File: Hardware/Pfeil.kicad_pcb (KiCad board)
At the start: 4 copper layers, 50 x 13 mm, 49 parts, among them IC1 2536030320001, IC2 AP7312-1233FM-7, J3 TagConnect, U2 WSEN-PADS_2511020213301, U3 WSEN-PADS_2511020213301, U4 nRF52840, X2 XTAL 32.768kHz 9pF, X3 XTAL 32MHz 8pF

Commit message: Luca Berthold review
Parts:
- removed X3: XTAL 32MHz 8pF, Crystal:Crystal_SMD_2016-4Pin_2.0x1.6mm
- added X1: XTAL 32MHz 8pF, Crystal:Crystal_SMD_2016-4Pin_2.0x1.6mm, F.Cu at (134.8, 53.5)
- moved C7 3.60 mm to (170.8, 55.6), turned to 90 degrees
- moved C40 3.57 mm to (141.1, 52.9)
- moved C43 3.57 mm to (141.6, 53.4)
- moved C49 3.08 mm to (144.4, 53.9)
- moved C47 2.95 mm to (138.1, 52.9)
- moved C46 2.77 mm to (132.8, 59.4), turned to 45 degrees
- moved L5 2.57 mm to (144.9, 55.0), turned to 135 degrees
- moved C39 2.26 mm to (135.2, 55.8), turned to 45 degrees
- moved C10 2.03 mm to (159.0, 61.8)
- moved C11 2.03 mm to (159.0, 62.5)
- moved C12 2.03 mm to (163.8, 61.4)
- moved IC2 2.03 mm to (161.4, 62.0)
- moved ANT1 1.73 mm to (151.9, 53.1)
- moved C29 1.73 mm to (147.6, 54.0)
- moved C4 1.73 mm to (147.6, 53.2)
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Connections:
- C7 pad 1: /ISDS_INT_00 -> /VDD_IO
- IC1 pad 1: /ISDS_INT_00 -> /SAO
- IC1 pad 10: /RSVD0 -> unconnected-(IC1-RSVD_3-Pad10)
- IC1 pad 11: /RSVD1 -> unconnected-(IC1-RSVD_4-Pad11)
- IC1 pad 2: /ISDS_INT_00 -> /RSVD3
- IC1 pad 3: /ISDS_INT_00 -> /RSVD2
- IC1 pad 5: /ISDS_INT_00 -> /VDD_IO
- R5 pad 1: /ISDS_INT_00 -> /VDD_IO
- R5 pad 2: /ISDS_INT_00 -> /RSVD2
- R6 pad 1: /ISDS_INT_00 -> /VDD_IO
- R6 pad 2: /ISDS_INT_00 -> /RSVD3
- R7 pad 1: /ISDS_INT_00 -> /VDD_IO
- R7 pad 2: /ISDS_INT_00 -> /SAO
- R9 pad 1: /ISDS_INT -> /VDD_IO
- R9 pad 2: /ISDS_INT_00 -> /ISDS_INT
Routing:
- net GND: track 94.9 -> 11.3 mm, vias 12 -> 61
- net /ISDS_INT_00: track 15.1 -> 0.00 mm, vias 2 -> 0
- net /VDD_IO: track 0.00 -> 13.9 mm, vias 0 -> 2
- net /I2C_SDA A1: track 25.0 -> 16.7 mm
- net /I2C_SDA A2: track 30.3 -> 27.2 mm
- net +3V3: track 72.4 -> 69.5 mm
- net /FEEL: track 14.4 -> 12.3 mm
- net Net-(U4-XC1): track 2.89 -> 5.02 mm
- net Net-(U4-DEC6): track 3.89 -> 1.84 mm
- net Net-(U4-XC2): track 6.07 -> 4.19 mm
- net /RSVD2: track 0.00 -> 1.85 mm
- net /SAO: track 0.00 -> 1.83 mm
- net Net-(U4-DEC3): track 4.13 -> 2.53 mm
- net /RSVD3: track 0.00 -> 1.49 mm
- net Net-(U4-DEC2): track 1.64 -> 2.73 mm
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- added copper zone on B.Cu, net GND
- added copper zone on F.Cu, net GND
- added copper zone on In1.Cu, net GND
- added copper zone on In2.Cu, net GND
- removed copper zone on B.Cu, net (none)
- removed copper zone on F.Cu, net (none)
- removed copper zone on In1.Cu, net (none)
- removed copper zone on In2.Cu, net (none)

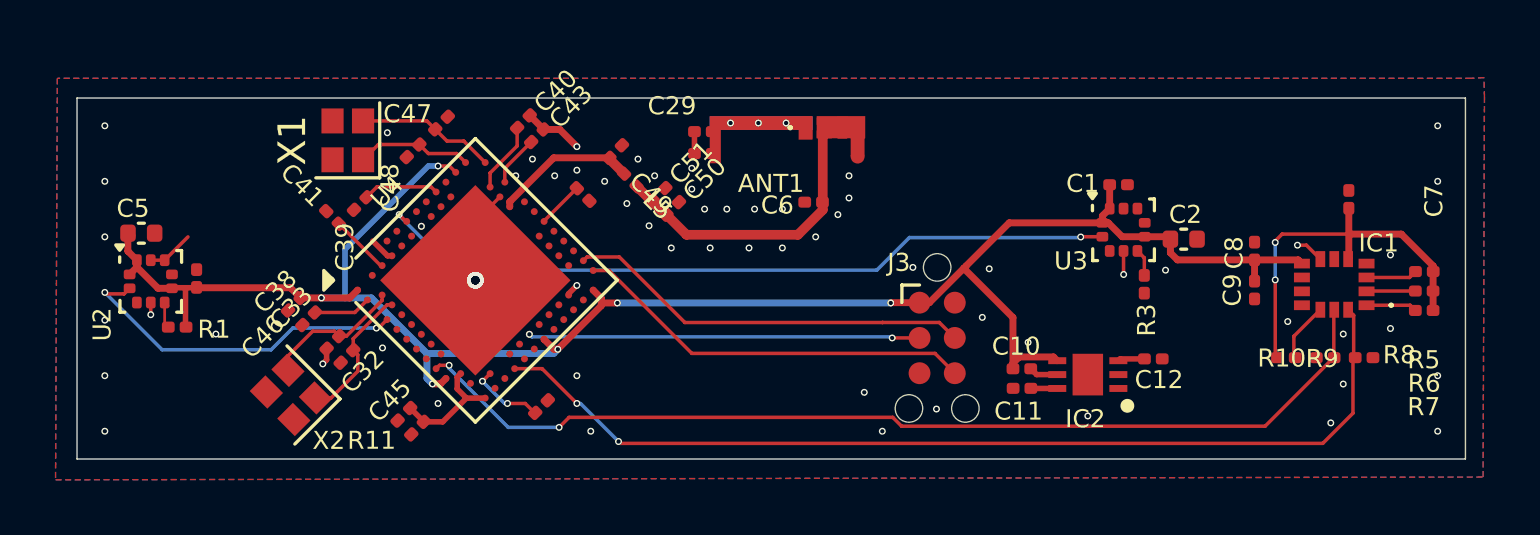
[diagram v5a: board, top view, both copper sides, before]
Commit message: Fix all sikscreen erros
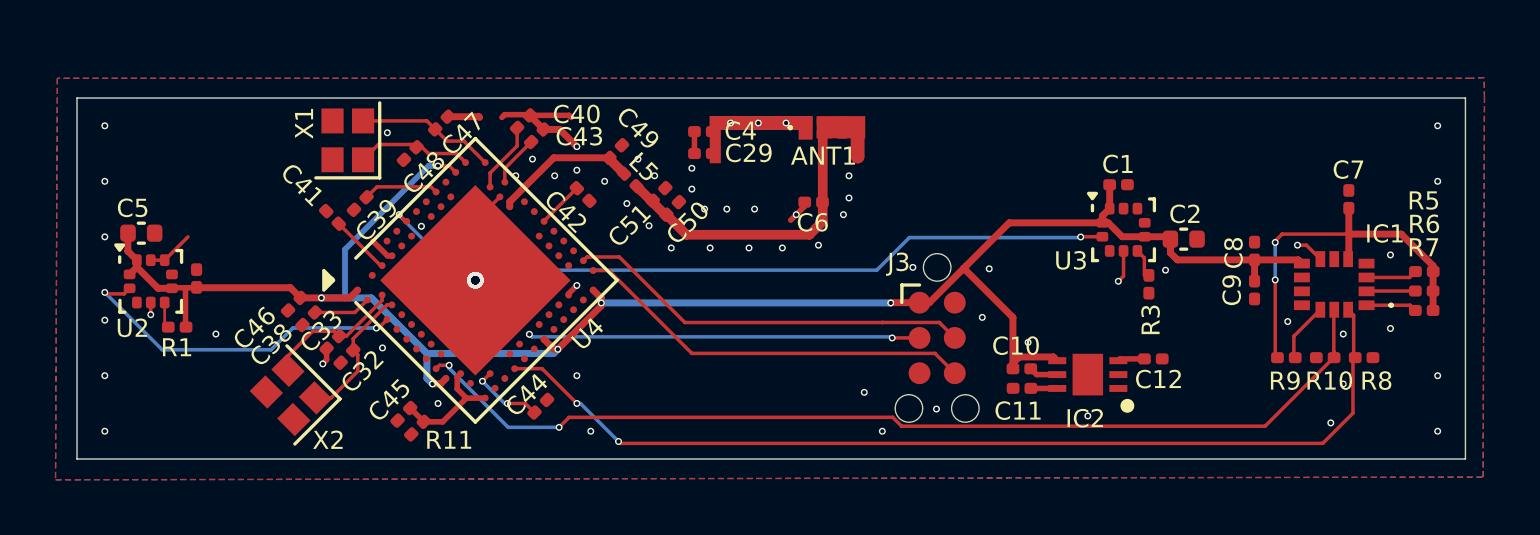
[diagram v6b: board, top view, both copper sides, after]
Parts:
- moved R3 0.16 mm to (163.6, 58.7)
- moved C48 0.14 mm to (137.0, 54.0)
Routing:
- net GND: track 11.3 -> 15.9 mm

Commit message: Bestellte version
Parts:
- added C13: 1uF, Capacitor_SMD:C_0805_2012Metric, F.Cu at (165.1, 62.5)
- added J1: Conn_01x01_Pin, Connector_Wire:SolderWirePad_1x01_SMD_1x2mm, B.Cu at (173.8, 63.1)
- added J2: Conn_01x01_Pin, Connector_Wire:SolderWirePad_1x01_SMD_1x2mm, F.Cu at (173.8, 63.1)
- C10, C11, C12: footprint Capacitor_SMD:C_0201_0603Metric -> Capacitor_SMD:C_0805_2012Metric
- C49: value 100nF -> N.C.
- C50: value 100nF -> 0.5pF NPO +10%
- C51: value 100nF -> 0.8pF NPO +10%
- L5: value L -> 4.7nH 5% HF; footprint Inductor_SMD:L_0201_0603Metric -> LED_SMD:LED_0402_1005Metric
- moved J3 6.71 mm to (149.3, 60.0), turned to 180 degrees
- moved C11 2.71 mm to (161.7, 62.9), turned to 0 degrees
- moved C12 1.61 mm to (165.1, 60.5)
- moved IC2 1.30 mm to (161.7, 60.7)
- moved NT1 0.85 mm to (153.7, 53.0), turned to 180 degrees
- moved C10 0.55 mm to (159.0, 61.2), turned to 90 degrees
- moved C50 0.47 mm to (146.8, 56.3)
- moved C51 0.47 mm to (146.3, 55.8)
- moved L5 0.27 mm to (145.2, 55.1)
- moved C49 0.06 mm to (144.4, 54.0)
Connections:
- IC2 pad 1: unconnected-(IC2-IN-Pad1) -> Net-(IC2-IN)
- U4 pad AD16: unconnected-(U4-P0.20-PadAD16) -> /ISDS_INT_00
- U4 pad AD18: unconnected-(U4-P0.22-PadAD18) -> /ISDS_INT_01
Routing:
- net /ISDS_INT_00: track 0.00 -> 33.3 mm, vias 0 -> 2
- net /ISDS_INT_01: track 0.00 -> 28.7 mm, vias 0 -> 2
- net Net-(IC2-IN): track 0.00 -> 12.0 mm, vias 0 -> 1
- net /SWDIO: track 14.6 -> 5.44 mm
- net GND: track 15.9 -> 23.4 mm, vias 61 -> 79
- net /SWCLK: track 14.6 -> 7.92 mm
- net +3V3: track 69.5 -> 75.5 mm, vias 6 -> 4
- net /RESET: track 14.1 -> 10.5 mm
- net Net-(IC2-OUT2): track 1.04 -> 2.43 mm
- net /I2C_SCL A1: track 12.5 -> 11.5 mm
- net Net-(IC2-OUT1): track 0.95 -> 1.76 mm
- net Net-(IC2-EN2): track 0.97 -> 1.47 mm
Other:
- board text added: "GND"
- board text added: "Moritz Hansen"
- board text added: "SMART ARROW"
- board text added: "V_IN"

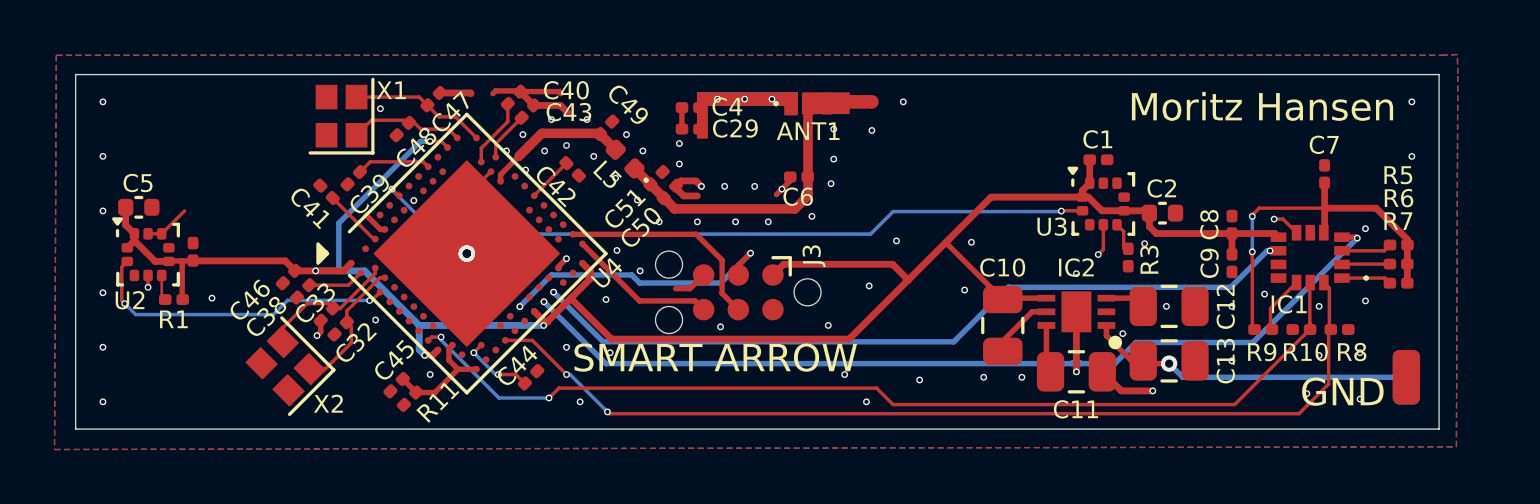
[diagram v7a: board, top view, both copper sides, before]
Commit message: change via size
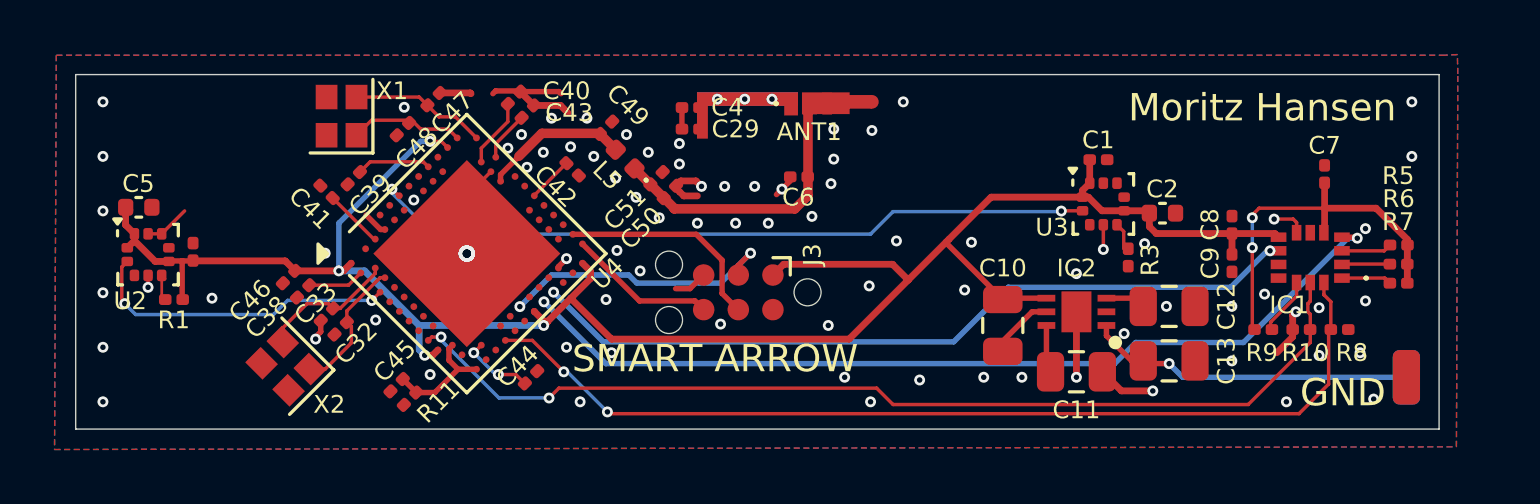
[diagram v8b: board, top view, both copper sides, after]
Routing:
- net GND: track 23.4 -> 25.6 mm, vias 79 -> 80
- net +3V3: track 75.5 -> 74.6 mm
